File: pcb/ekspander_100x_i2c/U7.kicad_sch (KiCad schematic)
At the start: 24 parts, among them J18 DG127A-5.08-06P-14-00AH, J19 DG127A-5.08-06P-14-00AH, J20 DG127A-5.08-06P-14-00AH, J21 DG127A-5.08-06P-14-00AH, J22 DG127A-5.08-06P-14-00AH, J23 DG127A-5.08-06P-14-00AH, U34 LTV-847, U35 ITS716G, U36 ITS716G, U37 LTV-847, U38 ITS716G, U39 ITS716G, U40 LTV-847, U41 LTV-847, U7 MCP23017_SP, U8 MCP23017_SP

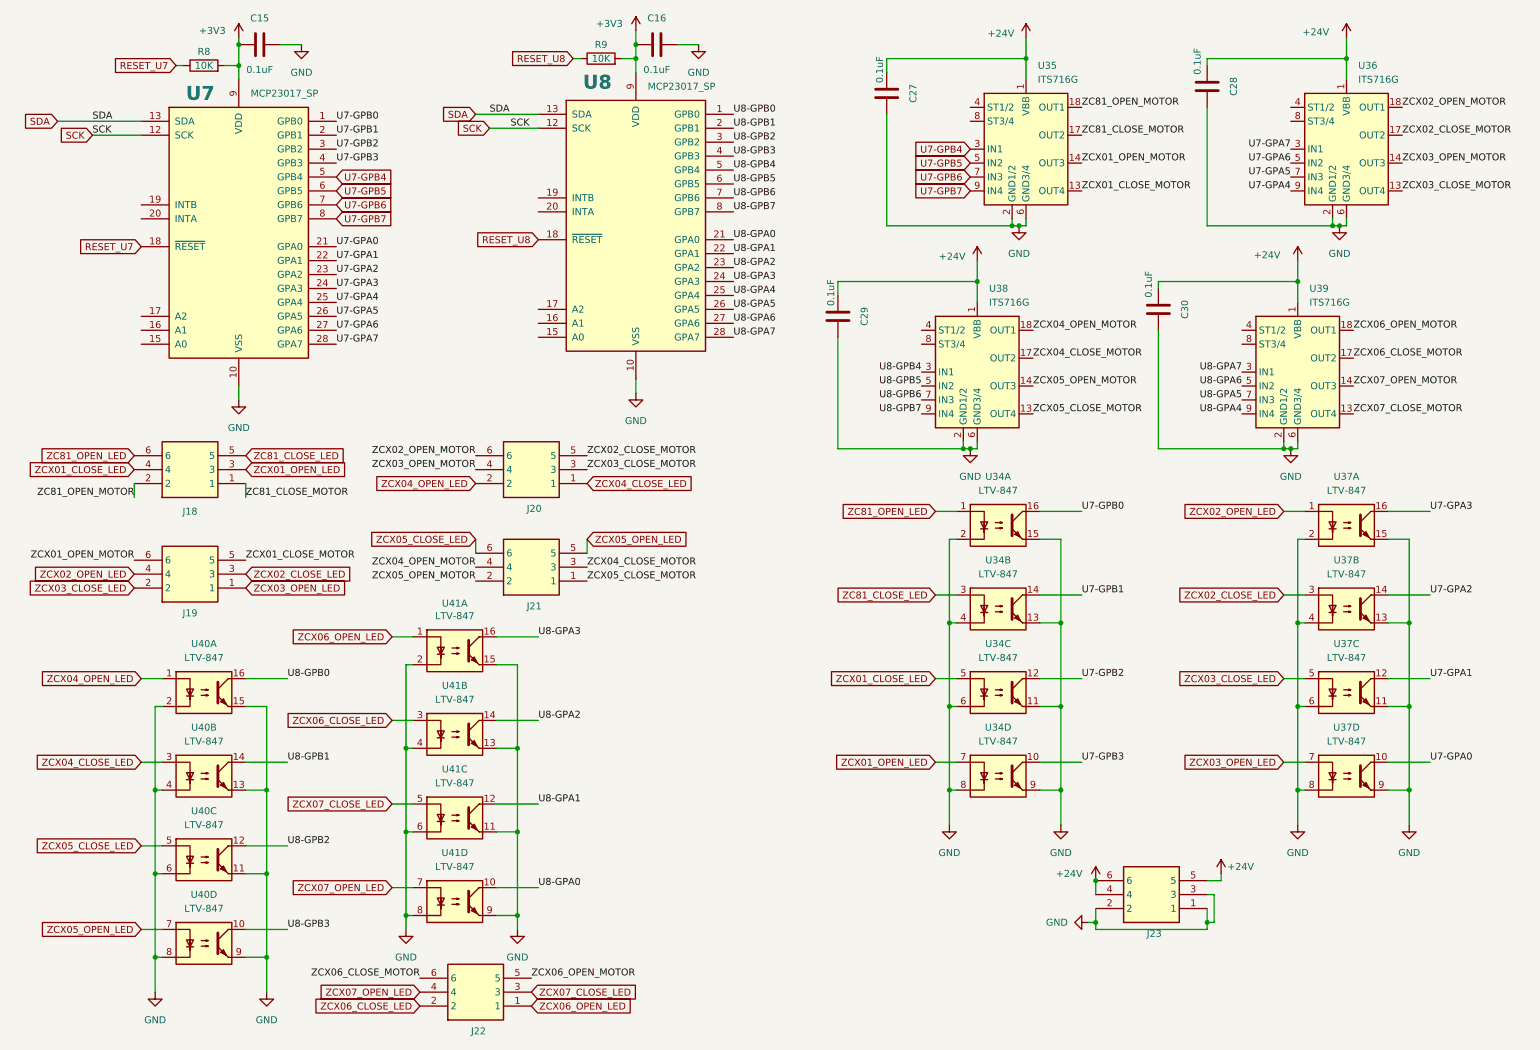
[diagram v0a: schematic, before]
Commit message: Ekspander 100x - finish J
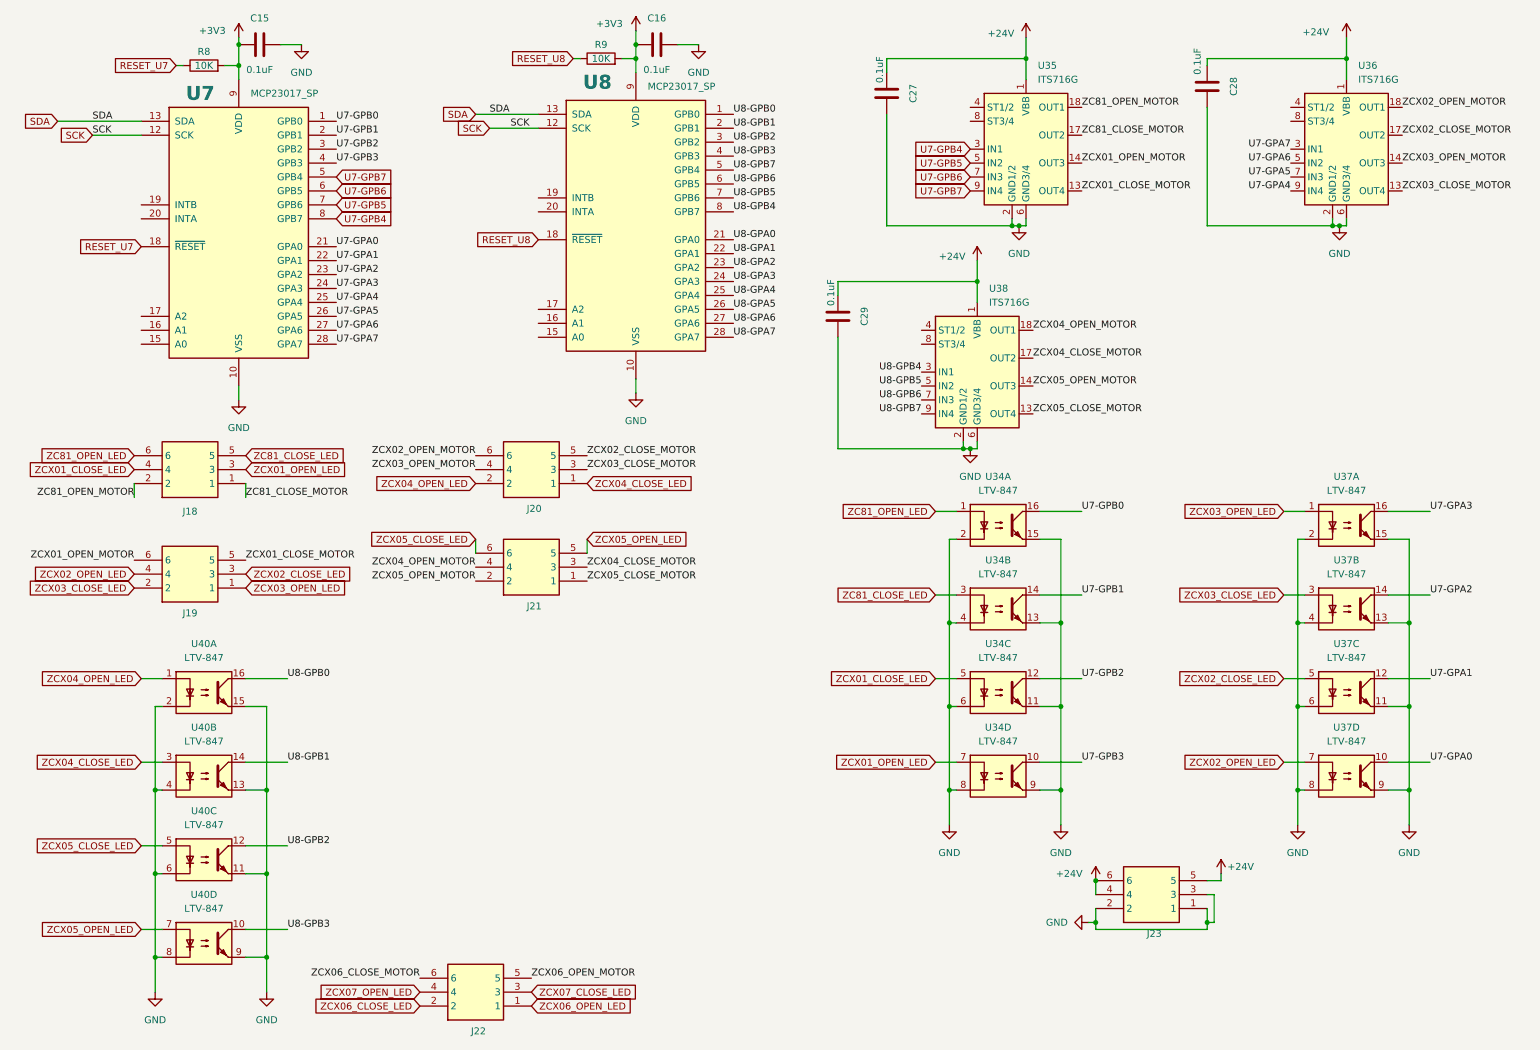
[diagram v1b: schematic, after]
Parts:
- removed C30: 0.1uF, Capacitor_SMD:C_0805_2012Metric_Pad1.18x1.45mm_HandSolder, symbol Device:C
- removed U39: ITS716G, Package_SO:SOIC-20W_7.5x12.8mm_P1.27mm, symbol Driver_FET:ITS716G
- removed U41: LTV-847, Package_DIP:DIP-16_W7.62mm, symbol Isolator:LTV-847
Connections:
- net U7-GPB4: now also U7.8 (GPB7); no longer U7.5 (GPB4)
- net U7-GPB5: now also U7.7 (GPB6); no longer U7.6 (GPB5)
- net U7-GPB6: now also U7.6 (GPB5); no longer U7.7 (GPB6)
- net U7-GPB7: now also U7.5 (GPB4); no longer U7.8 (GPB7)
- net U8-GPB4: now also U8.8 (GPB7); no longer U8.5 (GPB4)
- net U8-GPB5: now also U8.7 (GPB6); no longer U8.6 (GPB5)
- net U8-GPB6: now also U8.6 (GPB5); no longer U8.7 (GPB6)
- net U8-GPB7: now also U8.5 (GPB4); no longer U8.8 (GPB7)
- net ZCX02_CLOSE_LED: now also U37.5; no longer U37.3
- net ZCX02_OPEN_LED: now also U37.7; no longer U37.1
- net ZCX03_CLOSE_LED: now also U37.3; no longer U37.5
- net ZCX03_OPEN_LED: now also U37.1; no longer U37.7

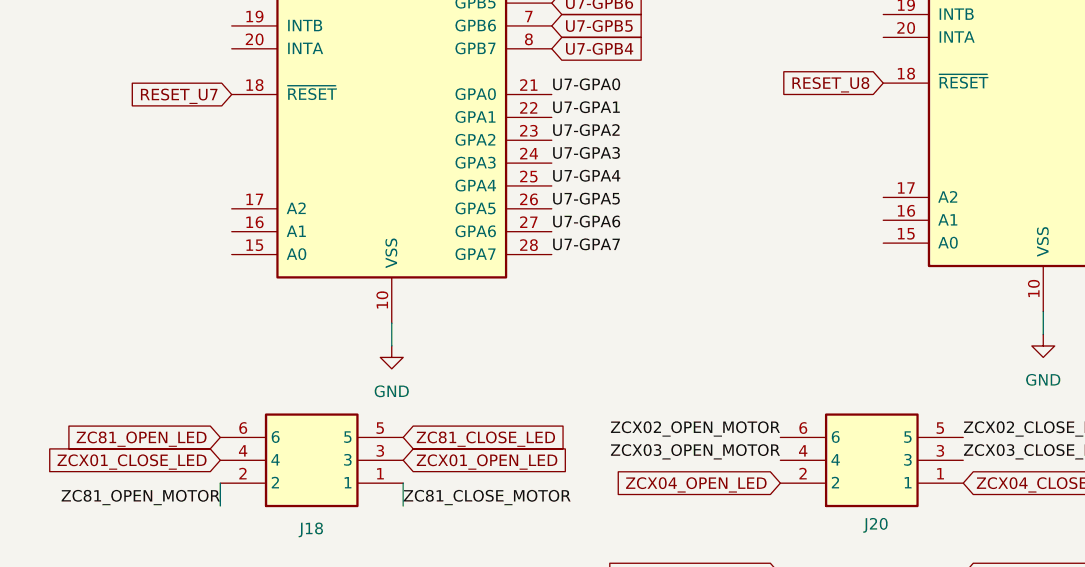
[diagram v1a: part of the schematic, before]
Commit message: Ekspander 100x - adresacja I2C - MCP23017
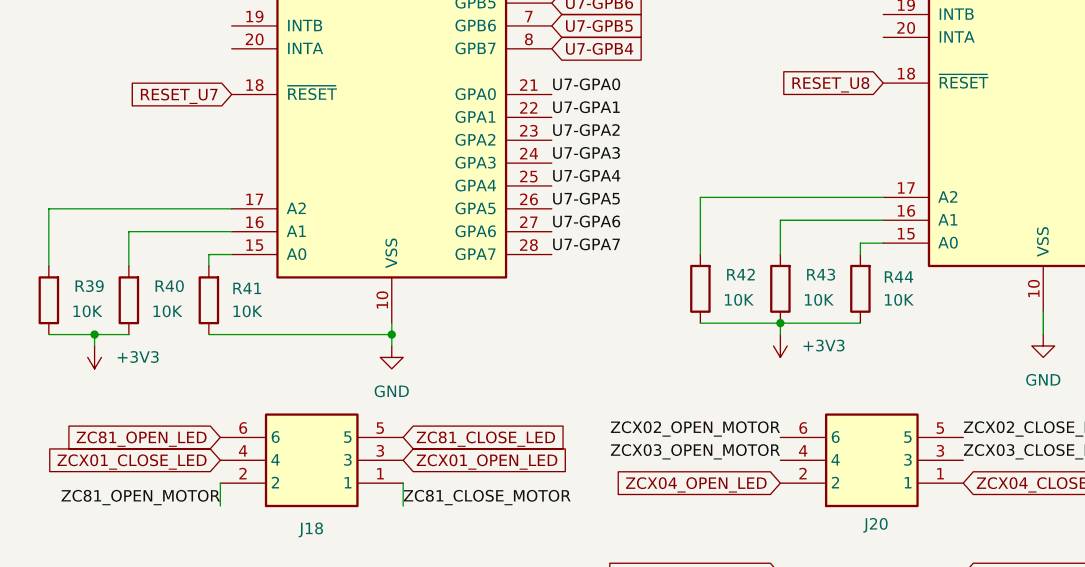
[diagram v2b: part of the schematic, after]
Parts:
- added R39, R40, R41, R42, R43, R44: 10K, PCM_Resistor_SMD_AKL:R_0805_2012Metric_Pad1.20x1.40mm_HandSolder, symbol Device:R
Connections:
- net +3V3: now also R39.1, R40.1, R42.1, R43.1, R44.1
- net GND: now also R41.1
- net at U8.15 (A0): now also R44.2
- net at U8.16 (A1): now also R43.2
- net at U8.17 (A2): now also R42.2
- net at U7.15 (A0): now also R41.2
- net at U7.16 (A1): now also R40.2
- net at U7.17 (A2): now also R39.2

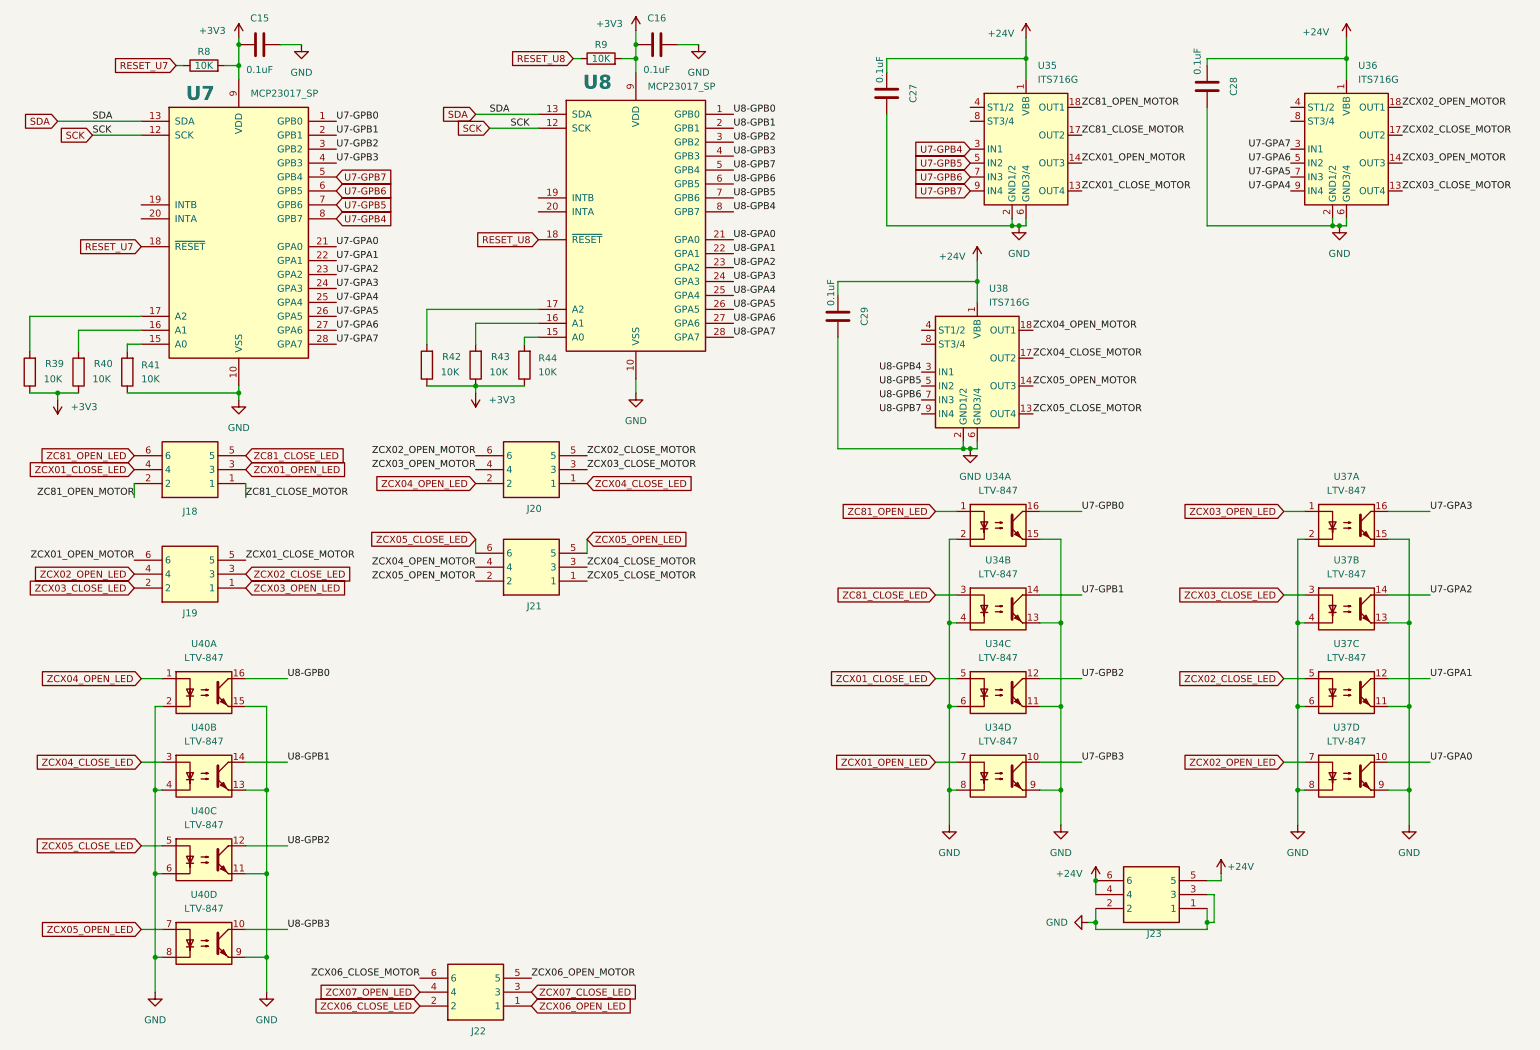
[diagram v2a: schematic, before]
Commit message: Ekspander 100x - diagnostic LEDs
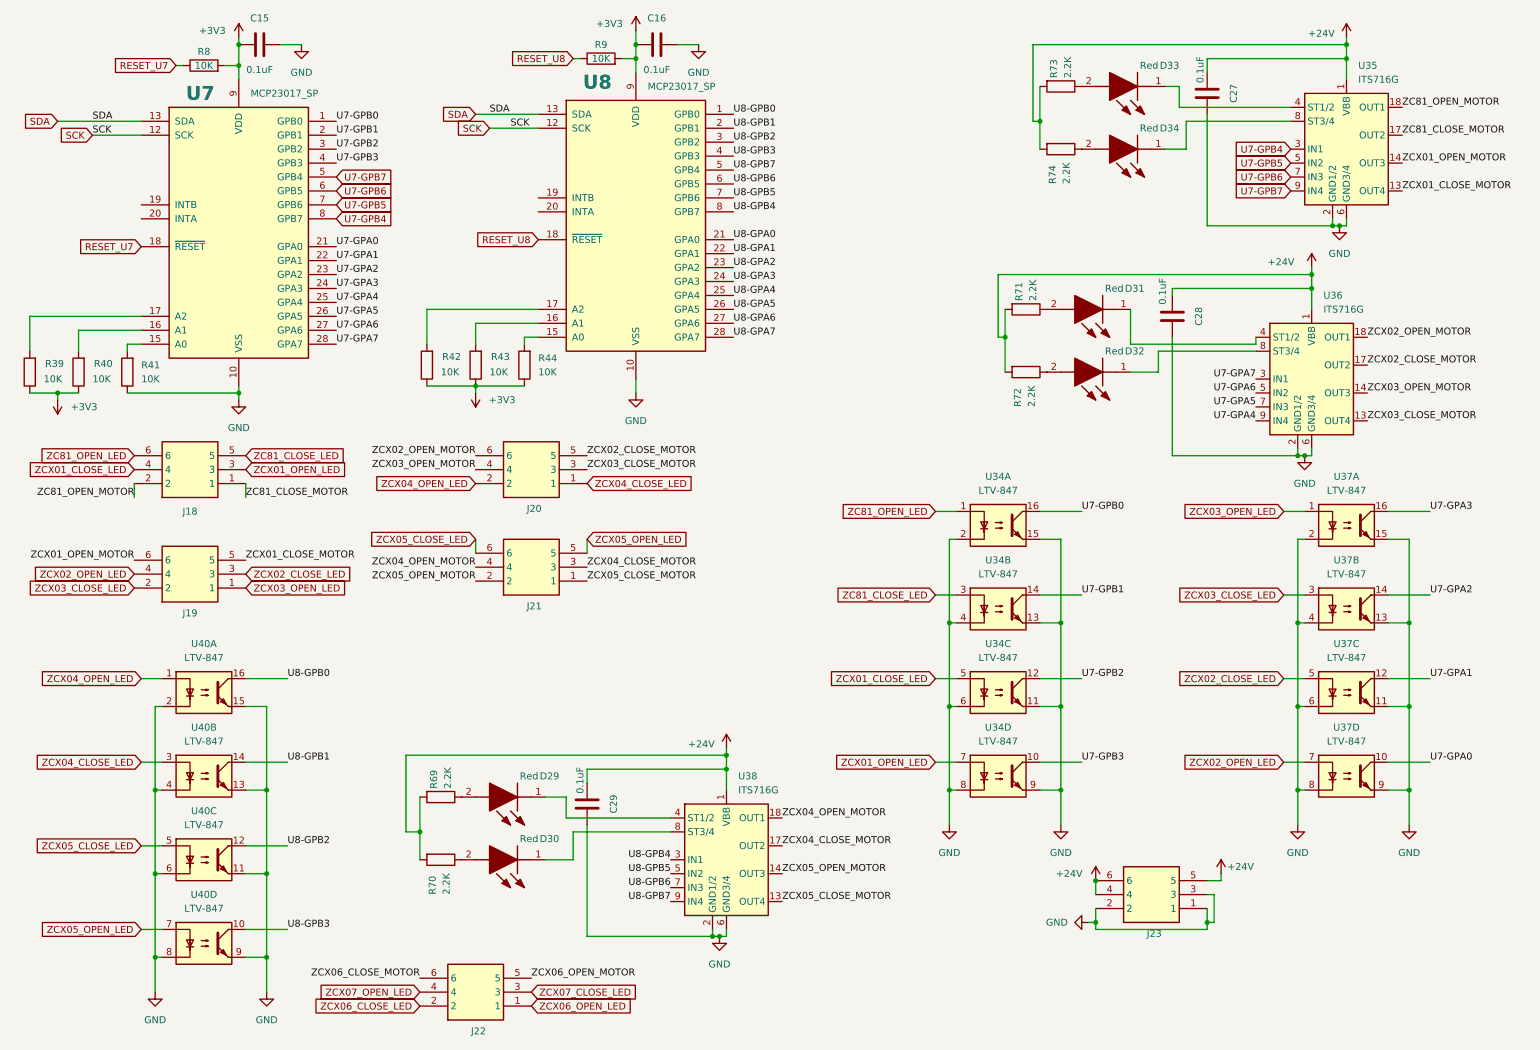
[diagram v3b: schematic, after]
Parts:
- added D29, D30, D31, D32, D33, D34: Red, 1_tme:LEDC2012X120N, symbol LTST-C170KRKT:LTST-C170KRKT
- added R69, R70, R71, R72, R73, R74: 2.2K, PCM_Resistor_SMD_AKL:R_0805_2012Metric_Pad1.20x1.40mm_HandSolder, symbol Device:R
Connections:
- net +24V: now also R69.2, R70.2, R71.2, R72.2, R73.2, R74.2
- net at U38.4 (ST1/2): now also D29.1 (K)
- net at U38.8 (ST3/4): now also D30.1 (K)
- net at U35.4 (ST1/2): now also D33.1 (K)
- net at U35.8 (ST3/4): now also D34.1 (K)
- net at U36.4 (ST1/2): now also D31.1 (K)
- net at U36.8 (ST3/4): now also D32.1 (K)
- new net: D32.2 (A), R72.1
- new net: D34.2 (A), R74.1
- new net: D30.2 (A), R70.1
- new net: D31.2 (A), R71.1
- new net: D29.2 (A), R69.1
- new net: D33.2 (A), R73.1
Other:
- moved on the sheet: C27, C28, C29, U35, U36, U38
